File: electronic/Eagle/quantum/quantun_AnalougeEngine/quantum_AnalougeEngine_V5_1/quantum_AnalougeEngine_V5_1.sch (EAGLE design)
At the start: 307 parts, among them IC1 OP275, IC10 STM32F767ZIT6, IC12 ESDA6V1BC6, IC13 USBLC6-4SC6, IC14 TL072, IC15 TL072, IC16 OP275, IC17 AD7606BSTZ-6, IC2 DAC084S085CIMM_NOPB, IC3 DAC084S085CIMM_NOPB, IC4 OP275, IC5 OP275, IC6 LAN8742A-CZ-TR, IC7 TL072, IC8 OP275, IC9 TL072, J1 GWLEX-SMT-S988G_Y, K1 Relay, K2 Relay, K3 Relay, K4 Relay, K5 Relay, K6 Relay, K7 Relay, K8 Relay, T1 H1102NL, U1 78_SMD, U12 ULN2003, U4 THAT1240, U6 THAT1240, U7 THAT1240, U8 THAT1240, Y1 NX3215SA-32.768K-STD-MUA-8, Y2 NX3225GD-8MHZ-STD-CRA-3, Y3 ABLS2-25.000MHZ-D4YF-T

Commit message: finished Routing: AnalougeEngine_V5_1
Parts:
- removed DISPLAY2: 90814-0204, electro_mechanical:90814-0204
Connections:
- removed net +5VVVV: R67.2
- net +5V: no longer DISPLAY2.3
- net +5V(ANALOG): now also R67.2
- net CHASIS: no longer C15.1, C18.1
- net CHASSIS: now also C15.1, C18.1
- net DISPLAY_GND_TO_STAR: no longer DISPLAY2.4
- net R/S_OUT+: now also C111.2
- net R/S_OUT-: no longer C111.2
- net USART1_RX: no longer DISPLAY2.2
- net USART1_TX: no longer DISPLAY2.1
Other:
- note removed: "display2 adapter"
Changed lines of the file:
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@@
 <part name="P-29" library="supply1" library_urn="urn:adsk.eagle:library:371" deviceset="V-" device="" value="-15V"/>
 <part name="INSERT_AFTER_GAIN" library="electro_mechanical" library_urn="urn:adsk.eagle:library:16388331" deviceset="90814-0204" device="" package3d_urn="urn:adsk.eagle:package:16762552/4"/>
-<part name="DISPLAY2" library="electro_mechanical" library_urn="urn:adsk.eagle:library:16388331" deviceset="90814-0204" device="" package3d_urn="urn:adsk.eagle:package:16762552/4"/>
-<part name="P+38" library="supply1" library_urn="urn:adsk.eagle:library:371" deviceset="+5V" device=""/>
 <part name="TP03" library="C_Sager_Bibliothek" library_urn="urn:adsk.eagle:library:560098" deviceset="TP" device="THT" package3d_urn="urn:adsk.eagle:package:817866/3"/>
 <part name="TP04" library="C_Sager_Bibliothek" library_urn="urn:adsk.eagle:library:560098" deviceset="TP" device="THT" package3d_urn="urn:adsk.eagle:package:817866/3"/>
@@
 <part name="P+32" library="supply1" library_urn="urn:adsk.eagle:library:371" deviceset="V+" device="" value="+15V"/>
 <part name="P+33" library="supply1" library_urn="urn:adsk.eagle:library:371" deviceset="V+" device="" value="+15V"/>
+<part name="U$15" library="supply" library_urn="urn:adsk.eagle:library:20637211" deviceset="CHASSIS" device=""/>
+<part name="U$16" library="supply" library_urn="urn:adsk.eagle:library:20637211" deviceset="CHASSIS" device=""/>
 </parts>
 <sheets>
@@
 <attribute name="VALUE" x="96.139" y="72.644" size="1.778" layer="96" rot="R90"/>
 </instance>
+<instance part="U$15" gate="G$1" x="137.16" y="129.54" smashed="yes"/>
 </instances>
 <busses>
@@
 <pinref part="OUT_RIGHT" gate="G$1" pin="OUT+"/>
 <wire x1="101.6" y1="66.04" x2="106.68" y2="66.04" width="0.1524" layer="91"/>
-<wire x1="106.68" y1="73.66" x2="106.68" y2="66.04" width="0.1524" layer="91"/>
+<wire x1="106.68" y1="76.2" x2="106.68" y2="66.04" width="0.1524" layer="91"/>
 <junction x="106.68" y="66.04"/>
 <wire x1="106.68" y1="66.04" x2="106.68" y2="50.8" width="0.1524" layer="91"/>
@@
 <wire x1="106.68" y1="50.8" x2="121.92" y2="50.8" width="0.1524" layer="91"/>
 <wire x1="121.92" y1="50.8" x2="121.92" y2="53.34" width="0.1524" layer="91"/>
+<pinref part="C111" gate="C$1" pin="2"/>
+<wire x1="96.52" y1="76.2" x2="106.68" y2="76.2" width="0.1524" layer="91"/>
 </segment>
 </net>
@@
 <wire x1="101.6" y1="55.88" x2="104.14" y2="55.88" width="0.1524" layer="91"/>
 <wire x1="104.14" y1="45.72" x2="104.14" y2="55.88" width="0.1524" layer="91"/>
+<pinref part="C110" gate="C$1" pin="2"/>
+<wire x1="96.52" y1="45.72" x2="104.14" y2="45.72" width="0.1524" layer="91"/>
 <wire x1="104.14" y1="55.88" x2="104.14" y2="71.12" width="0.1524" layer="91"/>
 <junction x="104.14" y="55.88"/>
-<wire x1="104.14" y1="71.12" x2="121.92" y2="71.12" width="0.1524" layer="91"/>
 <pinref part="K2" gate="2" pin="S"/>
+<wire x1="104.14" y1="71.12" x2="121.92" y2="71.12" width="0.1524" layer="91"/>
 <wire x1="121.92" y1="71.12" x2="121.92" y2="73.66" width="0.1524" layer="91"/>
-<pinref part="C111" gate="C$1" pin="2"/>
-<wire x1="96.52" y1="76.2" x2="104.14" y2="76.2" width="0.1524" layer="91"/>
-<wire x1="104.14" y1="76.2" x2="104.14" y2="71.12" width="0.1524" layer="91"/>
-<junction x="104.14" y="71.12"/>
-<pinref part="C110" gate="C$1" pin="2"/>
-<wire x1="96.52" y1="45.72" x2="104.14" y2="45.72" width="0.1524" layer="91"/>
 </segment>
 </net>
@@
 </segment>
 </net>
-<net name="CHASIS" class="0">
-<segment>
-<wire x1="142.24" y1="134.62" x2="139.7" y2="134.62" width="0.1524" layer="91"/>
-<label x="139.7" y="134.62" size="1.778" layer="95" rot="MR0" xref="yes"/>
-<pinref part="C15" gate="C$1" pin="1"/>
-</segment>
-</net>
 <net name="N$3" class="0">
 <segment>
@@
 <wire x1="195.58" y1="76.2" x2="208.28" y2="76.2" width="0.1524" layer="91"/>
 </segment>
+<segment>
+<pinref part="U$15" gate="G$1" pin="CHASSIS"/>
+<pinref part="C15" gate="C$1" pin="1"/>
+<wire x1="137.16" y1="132.08" x2="137.16" y2="134.62" width="0.1524" layer="91"/>
+<wire x1="137.16" y1="134.62" x2="142.24" y2="134.62" width="0.1524" layer="91"/>
+</segment>
 </net>
 <net name="N$98" class="0">
@@
 <attribute name="VALUE" x="91.059" y="42.164" size="1.778" layer="96" rot="R90"/>
 </instance>
+<instance part="U$16" gate="G$1" x="134.62" y="129.54" smashed="yes"/>
 </instances>
 <busses>
@@
 </segment>
 </net>
-<net name="CHASIS" class="0">
-<segment>
-<wire x1="137.16" y1="134.62" x2="134.62" y2="134.62" width="0.1524" layer="91"/>
-<label x="134.62" y="134.62" size="1.778" layer="95" rot="MR0" xref="yes"/>
-<pinref part="C18" gate="C$1" pin="1"/>
-</segment>
-</net>
 <net name="N$9" class="0">
 <segment>
@@
 <wire x1="198.12" y1="78.74" x2="198.12" y2="76.2" width="0.1524" layer="91"/>
 </segment>
+<segment>
+<pinref part="U$16" gate="G$1" pin="CHASSIS"/>
+<pinref part="C18" gate="C$1" pin="1"/>
+<wire x1="134.62" y1="132.08" x2="134.62" y2="134.62" width="0.1524" layer="91"/>
+<wire x1="134.62" y1="134.62" x2="137.16" y2="134.62" width="0.1524" layer="91"/>
+</segment>
 </net>
 <net name="N$100" class="0">
@@
 <wire x1="388.62" y1="193.04" x2="322.58" y2="193.04" width="0.1524" layer="94" style="dashdot"/>
 <text x="322.58" y="185.42" size="6.4516" layer="94">display1 adapter</text>
-<wire x1="322.58" y1="226.06" x2="322.58" y2="195.58" width="0.1524" layer="94" style="dashdot"/>
-<wire x1="322.58" y1="195.58" x2="388.62" y2="195.58" width="0.1524" layer="94" style="dashdot"/>
-<wire x1="388.62" y1="195.58" x2="388.62" y2="226.06" width="0.1524" layer="94" style="dashdot"/>
-<wire x1="388.62" y1="226.06" x2="322.58" y2="226.06" width="0.1524" layer="94" style="dashdot"/>
-<text x="322.58" y="218.44" size="6.4516" layer="94">display2 adapter</text>
 </plain>
 <instances>
@@
 <attribute name="VALUE" x="42.799" y="80.264" size="1.778" layer="96" rot="R90"/>
 </instance>
-<instance part="DISPLAY2" gate="G$1" x="345.44" y="208.28" smashed="yes">
-<attribute name="NAME" x="350.266" y="214.63" size="1.778" layer="95" align="center-left"/>
-<attribute name="VALUE" x="350.012" y="212.344" size="1.778" layer="96" align="center-left"/>
-</instance>
-<instance part="P+38" gate="1" x="370.84" y="215.9" smashed="yes">
-<attribute name="VALUE" x="368.3" y="213.36" size="1.778" layer="96" rot="R90"/>
-</instance>
 <instance part="TP05" gate="G$1" x="307.34" y="81.28" smashed="yes" rot="R270">
 <attribute name="NAME" x="308.61" y="80.01" size="1.778" layer="95"/>
@@
 <wire x1="375.92" y1="172.72" x2="375.92" y2="167.64" width="0.1524" layer="91"/>
 </segment>
-<segment>
-<pinref part="DISPLAY2" gate="G$1" pin="4"/>
-<wire x1="365.76" y1="205.74" x2="375.92" y2="205.74" width="0.1524" layer="91"/>
-<label x="375.92" y="200.66" size="1.778" layer="95" rot="R180" xref="yes"/>
-<wire x1="375.92" y1="205.74" x2="375.92" y2="200.66" width="0.1524" layer="91"/>
-</segment>
 </net>
 <net name="+5V" class="0">
@@
 <pinref part="P+34" gate="1" pin="+5V"/>
 </segment>
-<segment>
-<pinref part="DISPLAY2" gate="G$1" pin="3"/>
-<wire x1="370.84" y1="213.36" x2="370.84" y2="208.28" width="0.1524" layer="91"/>
-<wire x1="370.84" y1="208.28" x2="365.76" y2="208.28" width="0.1524" layer="91"/>
-<pinref part="P+38" gate="1" pin="+5V"/>
-</segment>
 </net>
 <net name="USART1_TX" class="0">
@@
 <label x="187.96" y="203.2" size="1.016" layer="95" rot="R90" xref="yes"/>
 </segment>
-<segment>
-<pinref part="DISPLAY2" gate="G$1" pin="1"/>
-<wire x1="345.44" y1="208.28" x2="342.9" y2="208.28" width="0.1524" layer="91"/>
-<label x="342.9" y="208.28" size="1.016" layer="95" rot="MR0" xref="yes"/>
-</segment>
 </net>
 <net name="USART1_RX" class="0">
@@
 <label x="276.86" y="88.9" size="1.016" layer="95" xref="yes"/>
 </segment>
-<segment>
-<pinref part="DISPLAY2" gate="G$1" pin="2"/>
-<wire x1="345.44" y1="205.74" x2="342.9" y2="205.74" width="0.1524" layer="91"/>
-<label x="342.9" y="205.74" size="1.016" layer="95" rot="MR0" xref="yes"/>
-</segment>
 </net>
 <net name="PB12" class="0">
@@
 </segment>
 </net>
-<net name="+5VVVV" class="0">
-<segment>
-<pinref part="R67" gate="G$1" pin="2"/>
-<wire x1="12.7" y1="76.2" x2="12.7" y2="78.74" width="0.1524" layer="91"/>
-<pinref part="U$5" gate="G$1" pin="+5V(ANALOG)"/>
-</segment>
-</net>
 <net name="+5V(ANALOG)" class="0">
 <segment>
@@
 <label x="172.72" y="152.4" size="1.778" layer="95"/>
 </segment>
+<segment>
+<pinref part="R67" gate="G$1" pin="2"/>
+<wire x1="12.7" y1="76.2" x2="12.7" y2="78.74" width="0.1524" layer="91"/>
+<pinref part="U$5" gate="G$1" pin="+5V(ANALOG)"/>
+</segment>
 </net>

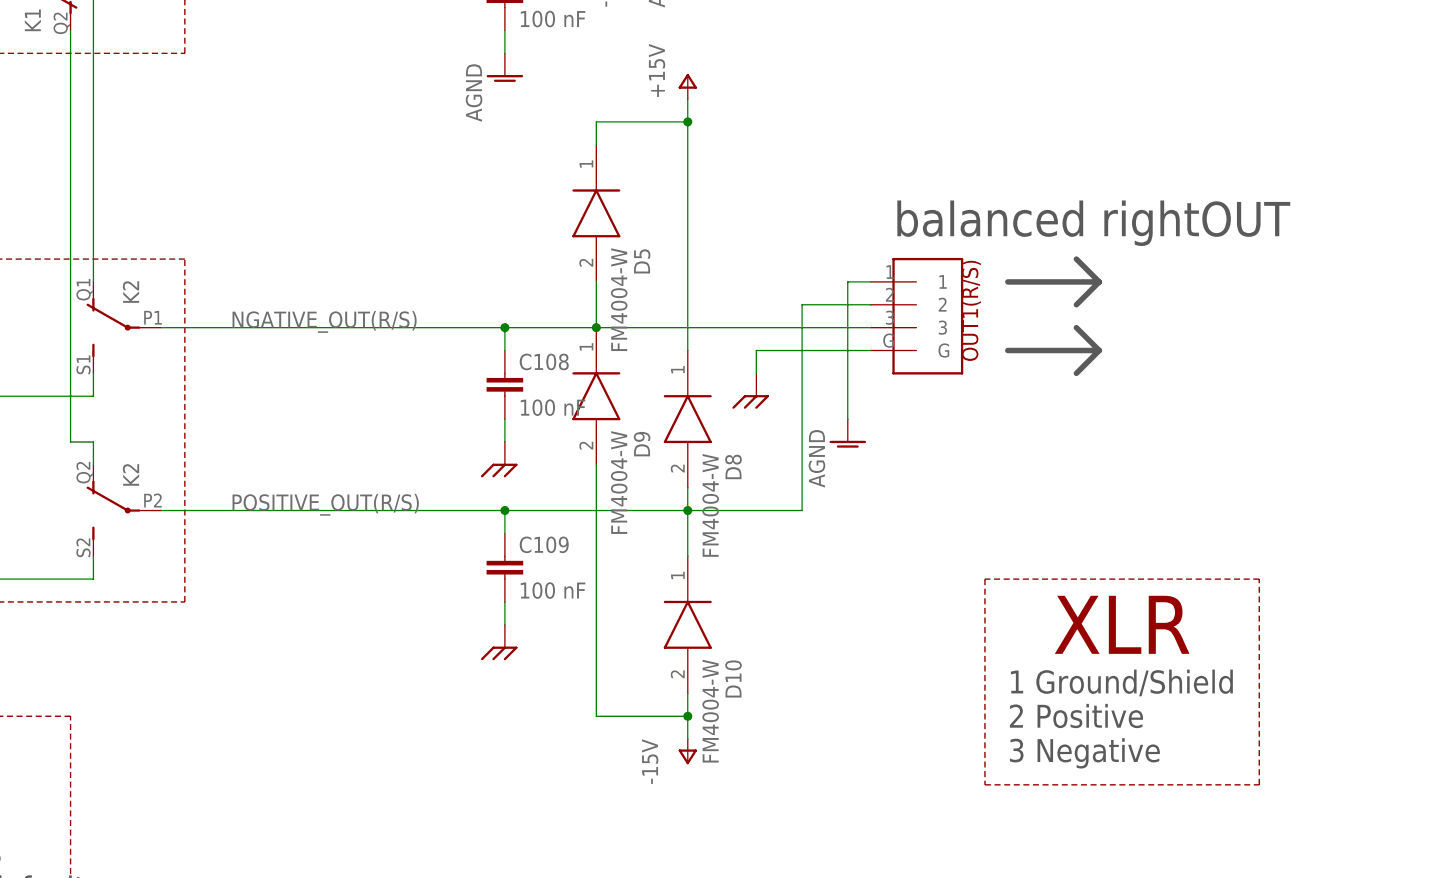
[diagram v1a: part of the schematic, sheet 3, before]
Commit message: finished all boards s for next PCBway production
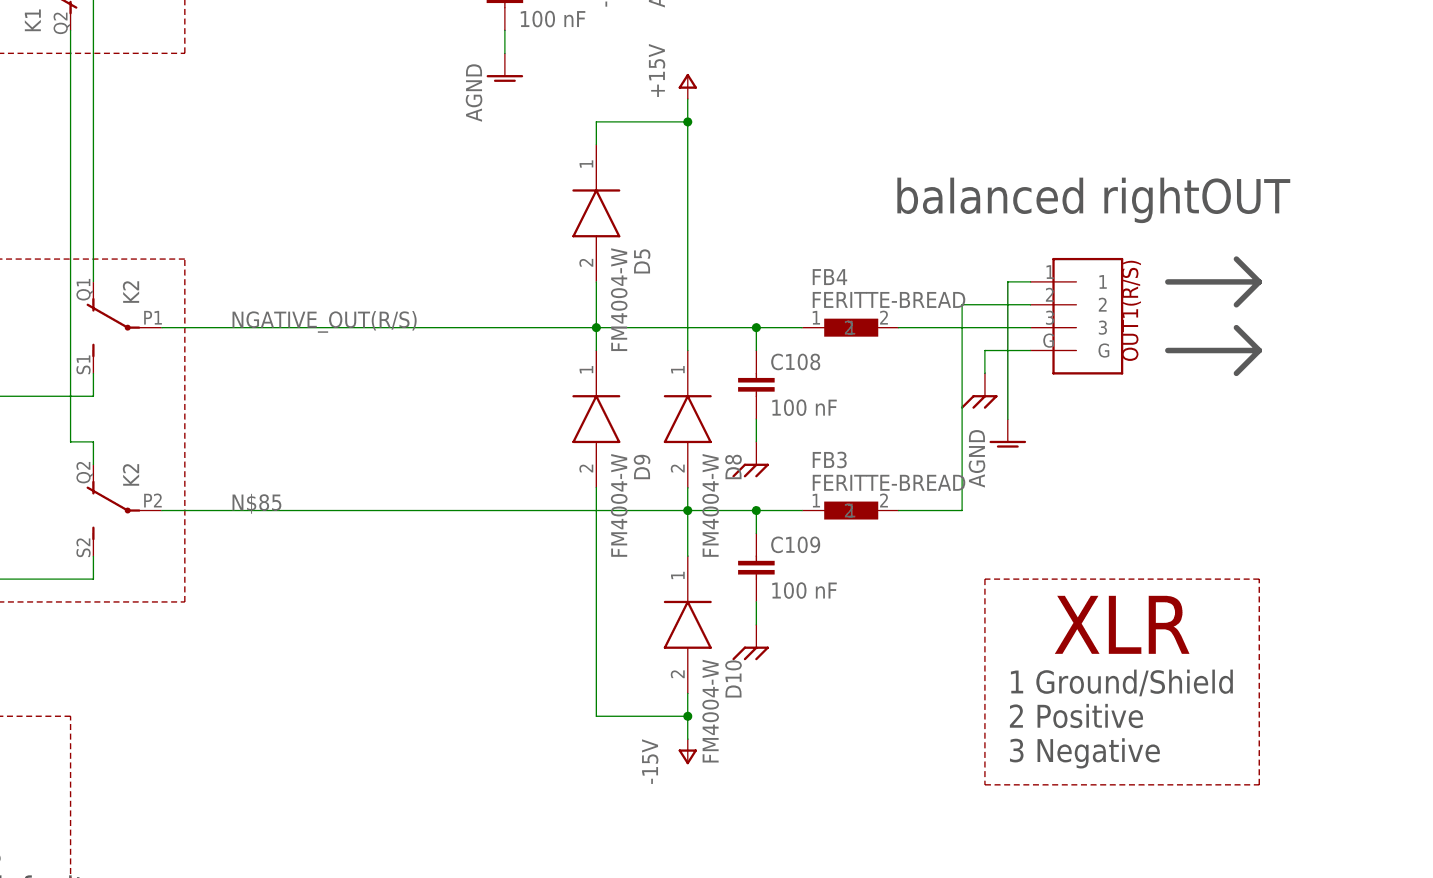
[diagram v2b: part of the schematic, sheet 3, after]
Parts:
- added FB1, FB2, FB3, FB4, FB6: FERITTE-BREAD, passive components:FERITTE-BREAD
- added FB5: 0 R, passive components:FERITTE-BREAD
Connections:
- removed net +12V: DIGITAL_VOLT.2
- new net N$106: C80.2, FB6.2, IC10.VDDA, IC10.VREF+
- new net N$41: C94.2, FB5.2, IC13.VBUS, R79.2, R80.2, R81.2, R82.2
- new net N$42: FB1.2, OUT2(L/M).3
- new net N$44: FB4.2, OUT1(R/S).3
- new net N$47: C107.1, D2.A, D3.K, FB2.1, K33.P
- new net N$85: C109.1, D10.K, D8.A, FB3.1, K23.P
- net +3V3: now also FB5.1, FB6.1; no longer C80.2, C94.2, IC10.VDDA, IC10.VREF+, IC13.VBUS, R79.2, R80.2, R81.2, R82.2
- net NEGATIVE_OUT(L/M): now also FB1.1; no longer OUT2(L/M).3
- net NGATIVE_OUT(R/S): now also FB4.1; no longer OUT1(R/S).3
- net POSITIVE_OUT(L/M): now also FB2.2; no longer C107.1, D2.A, D3.K, K33.P
- net POSITIVE_OUT(R/S): now also FB3.2; no longer C109.1, D10.K, D8.A, K23.P
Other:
- moved on the sheet: C105, C106, C107, C108, C109, D9, OUT1(R/S), OUT2(L/M)
